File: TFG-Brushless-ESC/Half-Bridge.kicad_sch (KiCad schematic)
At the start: 19 parts, among them Q5 TK58E06N1, Q6 TK58E06N1, U8 IR2101, U9 INA180A3

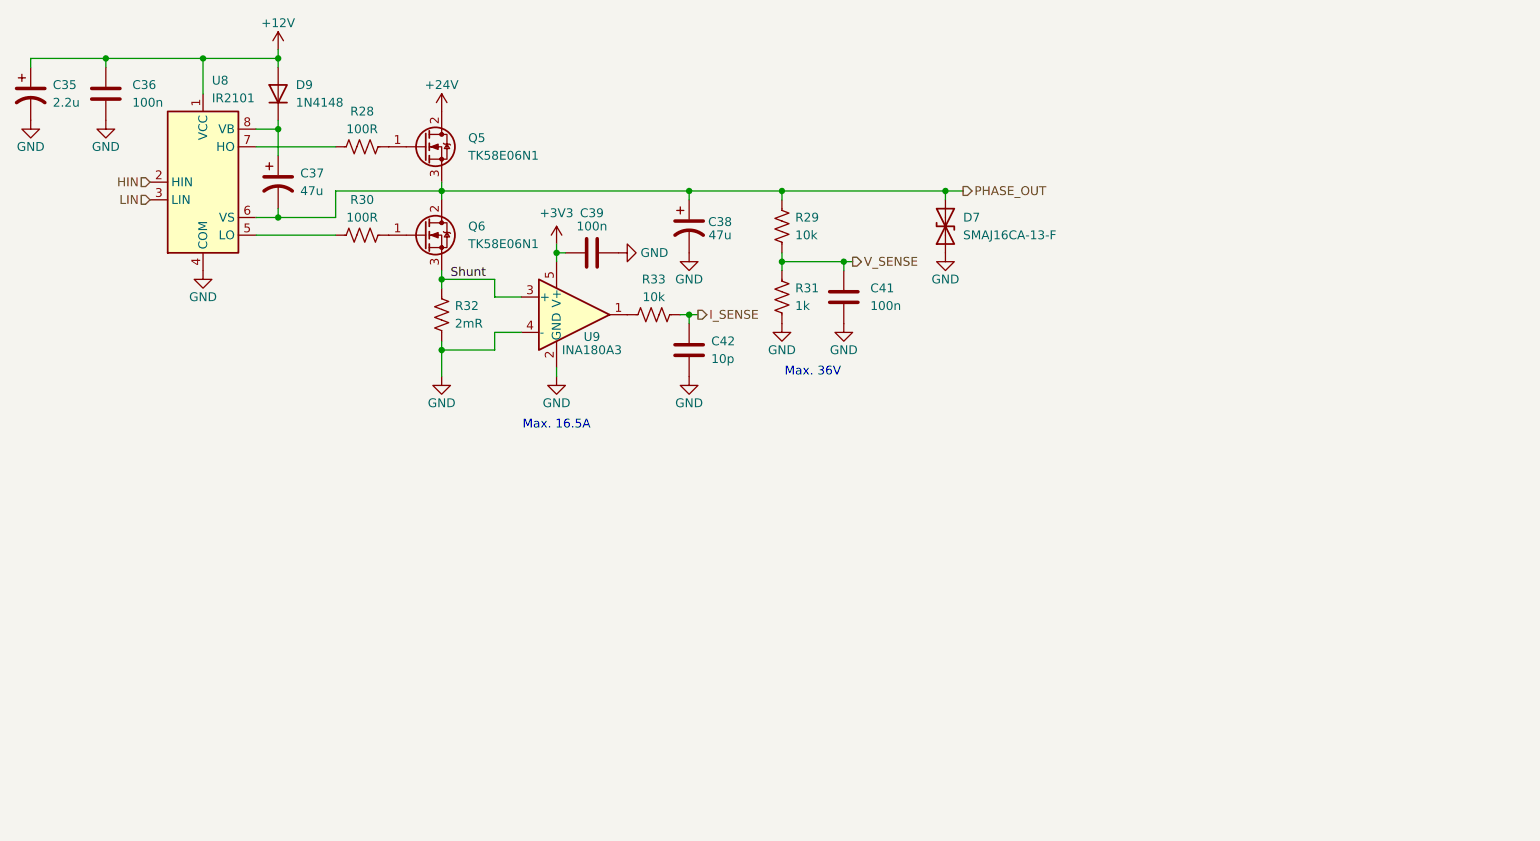
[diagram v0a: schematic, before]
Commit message: updated code to match pinout
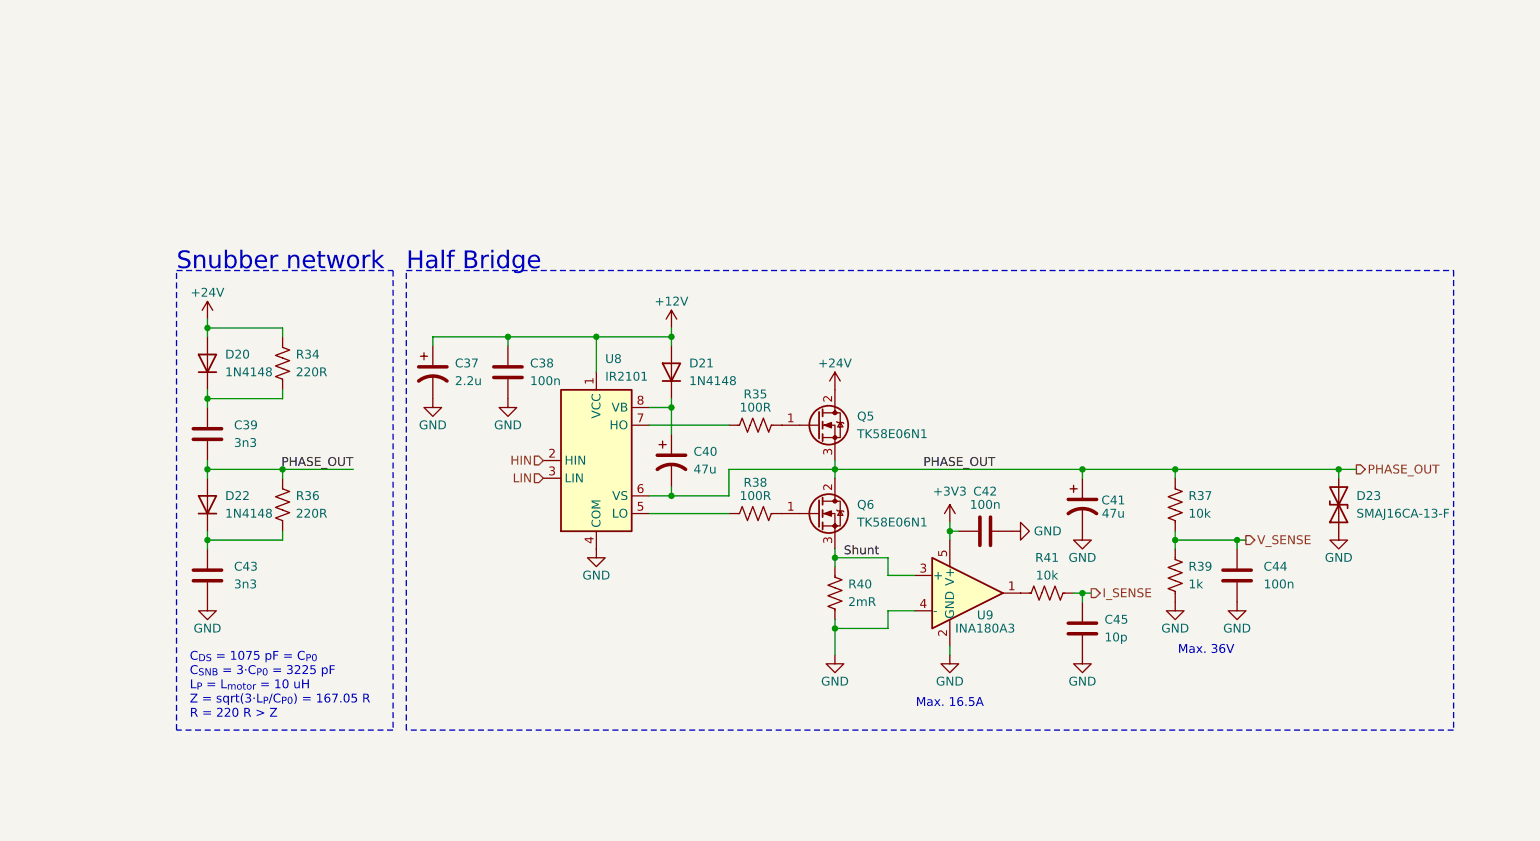
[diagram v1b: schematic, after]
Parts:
- added C39, C43: 3n3, Capacitor_SMD:C_0603_1608Metric, symbol Device:C
- added D20, D22: 1N4148, Diode_SMD:D_SOD-123, symbol Device:D
- added R34, R36: 220R, Resistor_SMD:R_0603_1608Metric, symbol Device:R_US
- C37: renamed from C35; footprint Capacitor_THT:CP_Radial_D5.0mm_P2.00mm -> Capacitor_SMD:CP_Elec_4x5.4
- C40: renamed from C37; footprint Capacitor_THT:CP_Radial_D5.0mm_P2.00mm -> Capacitor_SMD:CP_Elec_4x5.4
- C41: renamed from C38; footprint Capacitor_THT:CP_Radial_D5.0mm_P2.00mm -> Capacitor_SMD:CP_Elec_4x5.4
- renumbered C36 to C38, C39 to C42, C41 to C44, C42 to C45, D9 to D21, D7 to D23, R28 to R35, R29 to R37, R30 to R38, R31 to R39, R32 to R40, R33 to R41
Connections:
- net +24V: now also D20.2 (A), R34.2
- net GND: now also C43.2
- net PHASE_OUT: now also C39.2, D22.2 (A), R36.2
- new net: C43.1, D22.1 (K), R36.1
- new net: C39.1, D20.1 (K), R34.1
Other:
- note added: "C_{DS} = 1075 pF = C_{P0} C_{SNB} = 3·C_{P0} = 3225 pF L_{P} = L_{motor} = 10 uH Z = sqrt(3·L_{P}/C_{P0}) = 167.05 R R = 220 R > Z"
- note added: "Half Bridge"
- note added: "Snubber network"
- moved on the sheet: C37, C38, C40, C41, C42, C44, C45, D21, D23, Q5, Q6, R35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

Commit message: Slight code changes
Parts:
- removed C41: 47u, Capacitor_SMD:CP_Elec_4x5.4, symbol Device:C_Polarized_US
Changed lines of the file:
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@@
 	)
 	(junction
-		(at 186.69 94.615)
-		(diameter 0)
-		(color 0 0 0 0)
-	)
-	(junction
 		(at 127.635 98.425)
 		(diameter 0)
@@
 	(wire
 		(pts
-			(xy 151.13 94.615) (xy 186.69 94.615)
-		)
-		(stroke
-			(width 0)
-			(type default)
-		)
-	)
-	(wire
-		(pts
 			(xy 71.755 74.295) (xy 60.96 74.295)
 		)
@@
 	(wire
 		(pts
-			(xy 186.69 94.615) (xy 200.025 94.615)
+			(xy 151.13 94.615) (xy 200.025 94.615)
 		)
 		(stroke
@@
 	(wire
 		(pts
-			(xy 186.69 94.615) (xy 186.69 95.885)
-		)
-		(stroke
-			(width 0)
-			(type default)
-		)
-	)
-	(wire
-		(pts
 			(xy 200.025 94.615) (xy 223.52 94.615)
 		)
@@
 	(symbol
 		(lib_id "power:GND")
-		(at 186.69 103.505 0)
-		(unit 1)
-		(exclude_from_sim no)
-		(in_bom yes)
-		(on_board yes)
-		(dnp no)
-		(property "Reference" "#PWR098"
-			(at 186.69 109.855 0)
-			(effects
-				(font
-					(size 1.27 1.27)
-				)
-				(hide yes)
-			)
-		)
-		(property "Value" "GND"
-			(at 186.69 107.315 0)
-			(effects
-				(font
-					(size 1.27 1.27)
-				)
-			)
-		)
-		(property "Footprint" ""
-			(at 186.69 103.505 0)
-			(effects
-				(font
-					(size 1.27 1.27)
-				)
-				(hide yes)
-			)
-		)
-		(property "Datasheet" ""
-			(at 186.69 103.505 0)
-			(effects
-				(font
-					(size 1.27 1.27)
-				)
-				(hide yes)
-			)
-		)
-		(property "Description" ""
-			(at 186.69 103.505 0)
-			(effects
-				(font
-					(size 1.27 1.27)
-				)
-				(hide yes)
-			)
-		)
-		(pin "1"
-		)
-		(instances
-			(project "TFG-Brushless-ESC"
-				(path "/fc8dd9a9-f99a-4338-8182-2c8b4b8ed6dd/211b6883-96c8-42a2-bec5-a4dfd4e56ba6"
-					(reference "#PWR098")
-					(unit 1)
-				)
-				(path "/fc8dd9a9-f99a-4338-8182-2c8b4b8ed6dd/b5458e57-2ddd-4d30-9620-d640c1a391c8"
-					(reference "#PWR066")
-					(unit 1)
-				)
-				(path "/fc8dd9a9-f99a-4338-8182-2c8b4b8ed6dd/f6e668ab-a50d-4861-bee8-58a57ed6fcc7"
-					(reference "#PWR082")
-					(unit 1)
-				)
-			)
-		)
-	)
-	(symbol
-		(lib_id "power:GND")
 		(at 60.96 113.665 0)
 		(unit 1)
@@
 					(unit 1)
 				)
-			)
-		)
-	)
-	(symbol
-		(lib_id "Device:C_Polarized_US")
-		(at 186.69 99.695 0)
-		(unit 1)
-		(exclude_from_sim no)
-		(in_bom yes)
-		(on_board yes)
-		(dnp no)
-		(property "Reference" "C41"
-			(at 191.135 99.06 0)
-			(effects
-				(font
-					(size 1.27 1.27)
-				)
-			)
-		)
-		(property "Value" "47u"
-			(at 191.135 100.965 0)
-			(effects
-				(font
-					(size 1.27 1.27)
-				)
-			)
-		)
-		(property "Footprint" "Capacitor_SMD:CP_Elec_4x5.4"
-			(at 186.69 99.695 0)
-			(effects
-				(font
-					(size 1.27 1.27)
-				)
-				(hide yes)
-			)
-		)
-		(property "Datasheet" "~"
-			(at 186.69 99.695 0)
-			(effects
-				(font
-					(size 1.27 1.27)
-				)
-				(hide yes)
-			)
-		)
-		(property "Description" ""
-			(at 186.69 99.695 0)
-			(effects
-				(font
-					(size 1.27 1.27)
-				)
-				(hide yes)
-			)
-		)
-		(property "Sim.Device" "C"
-			(at 186.69 99.695 0)
-			(effects
-				(font
-					(size 1.27 1.27)
-				)
-				(hide yes)
-			)
-		)
-		(property "Sim.Pins" "1=+ 2=-"
-			(at 186.69 99.695 0)
-			(effects
-				(font
-					(size 1.27 1.27)
-				)
-				(hide yes)
-			)
-		)
-		(pin "1"
-		)
-		(pin "2"
-		)
-		(instances
-			(project "TFG-Brushless-ESC"
-				(path "/fc8dd9a9-f99a-4338-8182-2c8b4b8ed6dd/211b6883-96c8-42a2-bec5-a4dfd4e56ba6"
-					(reference "C41")
-					(unit 1)
-				)
-				(path "/fc8dd9a9-f99a-4338-8182-2c8b4b8ed6dd/b5458e57-2ddd-4d30-9620-d640c1a391c8"
-					(reference "C23")
-					(unit 1)
-				)
-				(path "/fc8dd9a9-f99a-4338-8182-2c8b4b8ed6dd/f6e668ab-a50d-4861-bee8-58a57ed6fcc7"
-					(reference "C32")
-					(unit 1)
-				)

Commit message: PCB v3
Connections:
- net VB: now reaches C40.1, D21.1 (K), U8.8 (VB)
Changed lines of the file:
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@@
+		)
+	)
+	(label "VB"
+		(at 125.095 85.725 0)
+		(effects
+			(font
+				(size 1.27 1.27)
+			)
+			(justify left bottom)
 		)
 	)

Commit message: Added fan control and temp measurement. Not added to pcb yet
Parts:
- added J6: ~, TFG-Brushless-ESC:Screw_Terminal, symbol Connector:Screw_Terminal_01x01
- added R42: 10k, Resistor_SMD:R_0603_1608Metric, symbol Device:R_US
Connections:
- net GND: now also R42.1
- net PHASE_OUT: now also J6.1 (Pin_1), R42.2

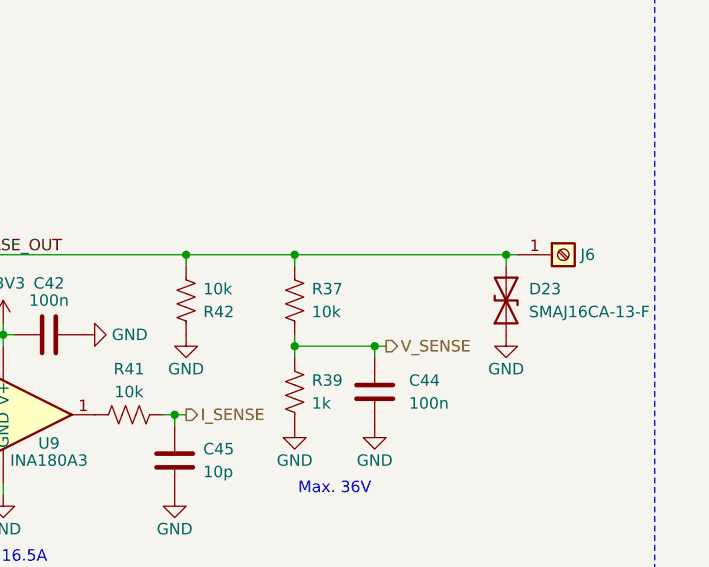
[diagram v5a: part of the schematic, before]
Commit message: Added temperature sensors per phase and adc
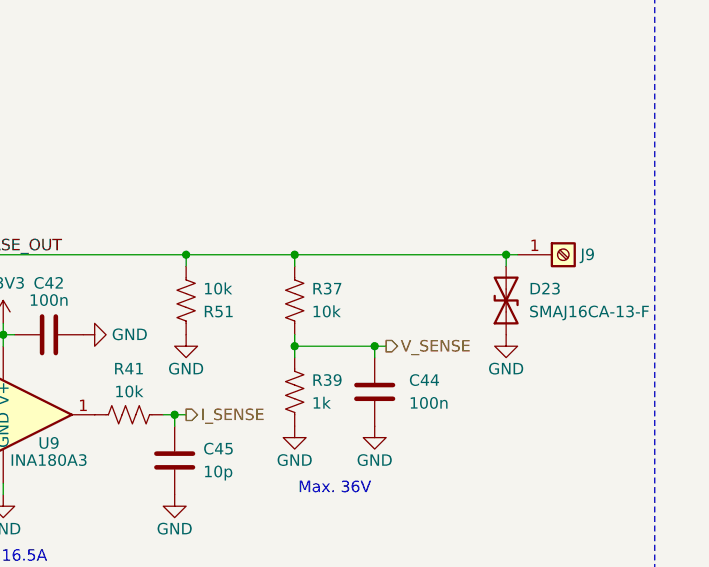
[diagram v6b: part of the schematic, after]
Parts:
- renumbered J6 to J9, R42 to R51
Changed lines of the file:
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@@
 		(on_board yes)
 		(dnp no)
-		(property "Reference" "#PWR0118"
+		(property "Reference" "#PWR0120"
 			(at 187.96 109.855 0)
 			(effects
@@
 		(on_board yes)
 		(dnp no)
-		(property "Reference" "J6"
+		(property "Reference" "J9"
 			(at 231.775 94.615 0)
 			(effects
@@
 		(on_board yes)
 		(dnp no)
-		(property "Reference" "R42"
+		(property "Reference" "R51"
 			(at 189.865 100.965 0)
 			(effects

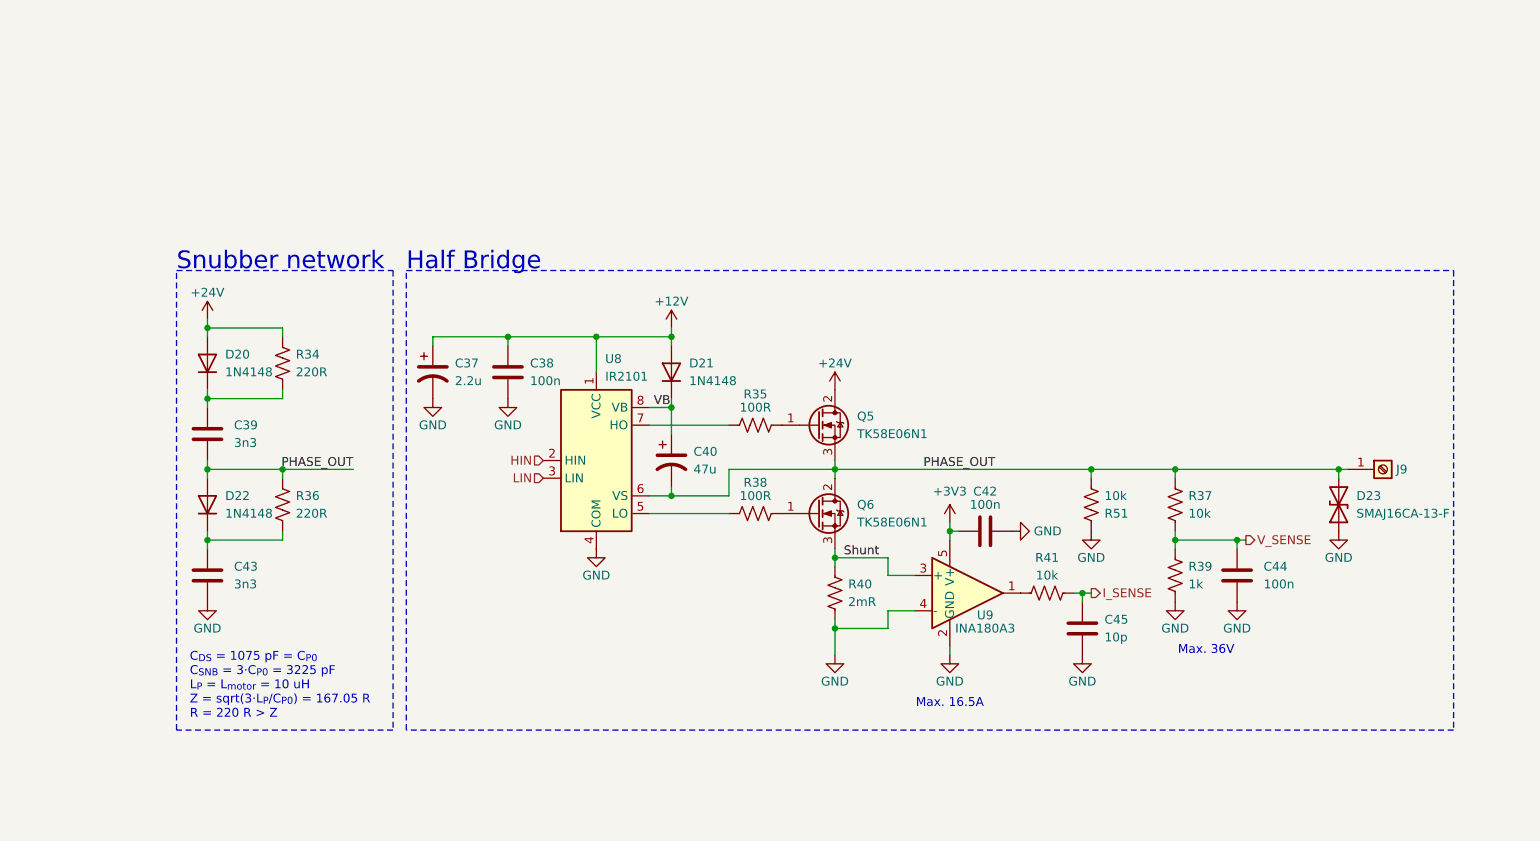
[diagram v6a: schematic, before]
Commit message: Added pulldown resistors for the half bridge mosfets, fan mosfet and fixed code pinout
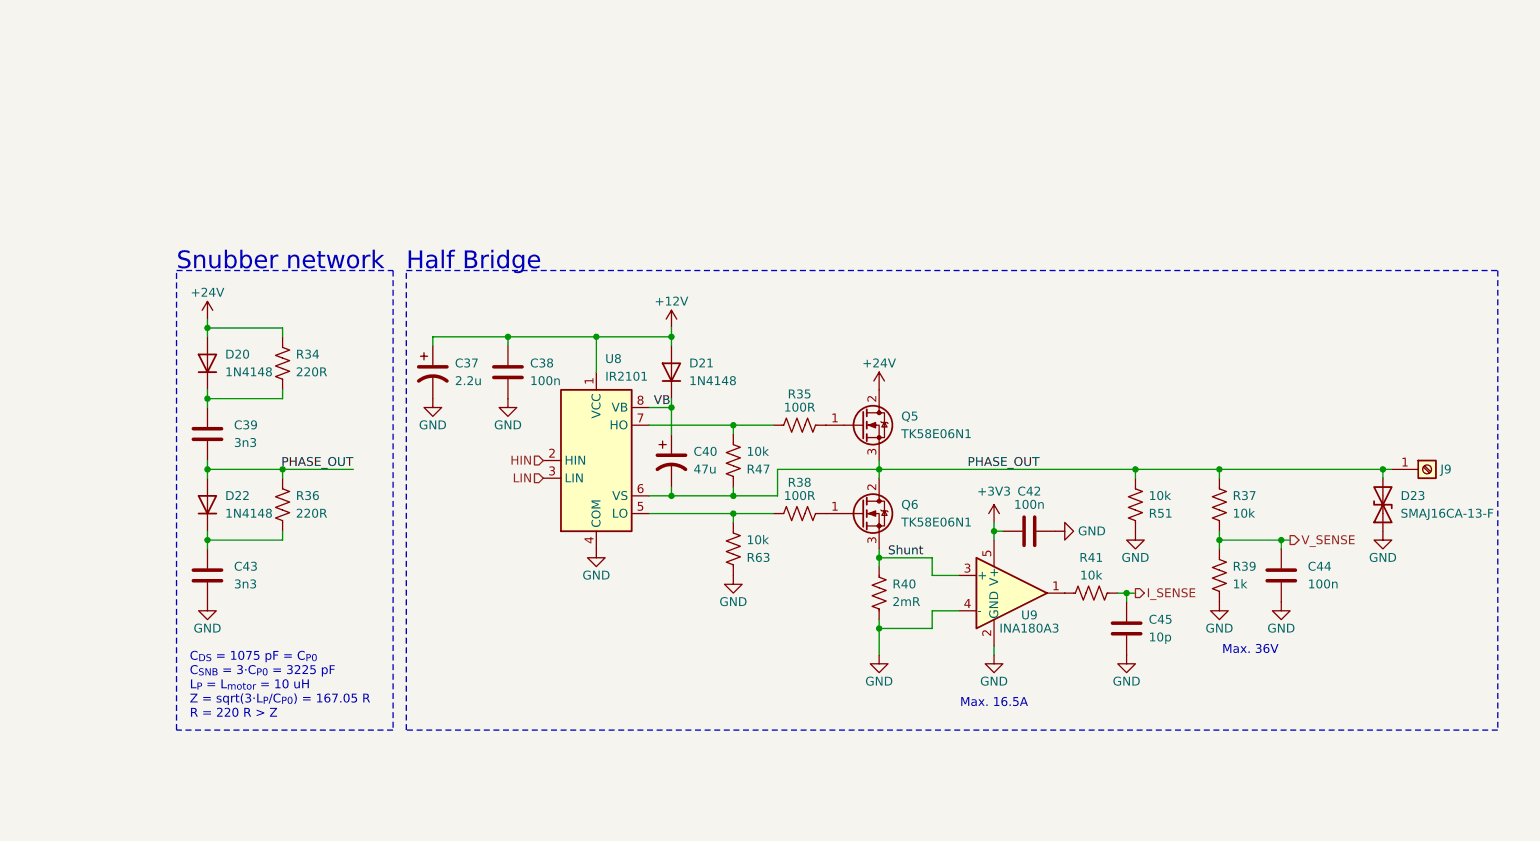
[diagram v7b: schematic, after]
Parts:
- added R47, R63: 10k, Resistor_SMD:R_0603_1608Metric, symbol Device:R_US
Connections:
- net GND: now also R63.1
- net PHASE_OUT: now also R47.1
- net at R38.1, U8.5 (LO): now also R63.2
- net at R35.1, U8.7 (HO): now also R47.2
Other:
- moved on the sheet: C42, C44, C45, D23, J9, Q5, Q6, R35, R37, R38, R39, R40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

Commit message: Traducción nombres
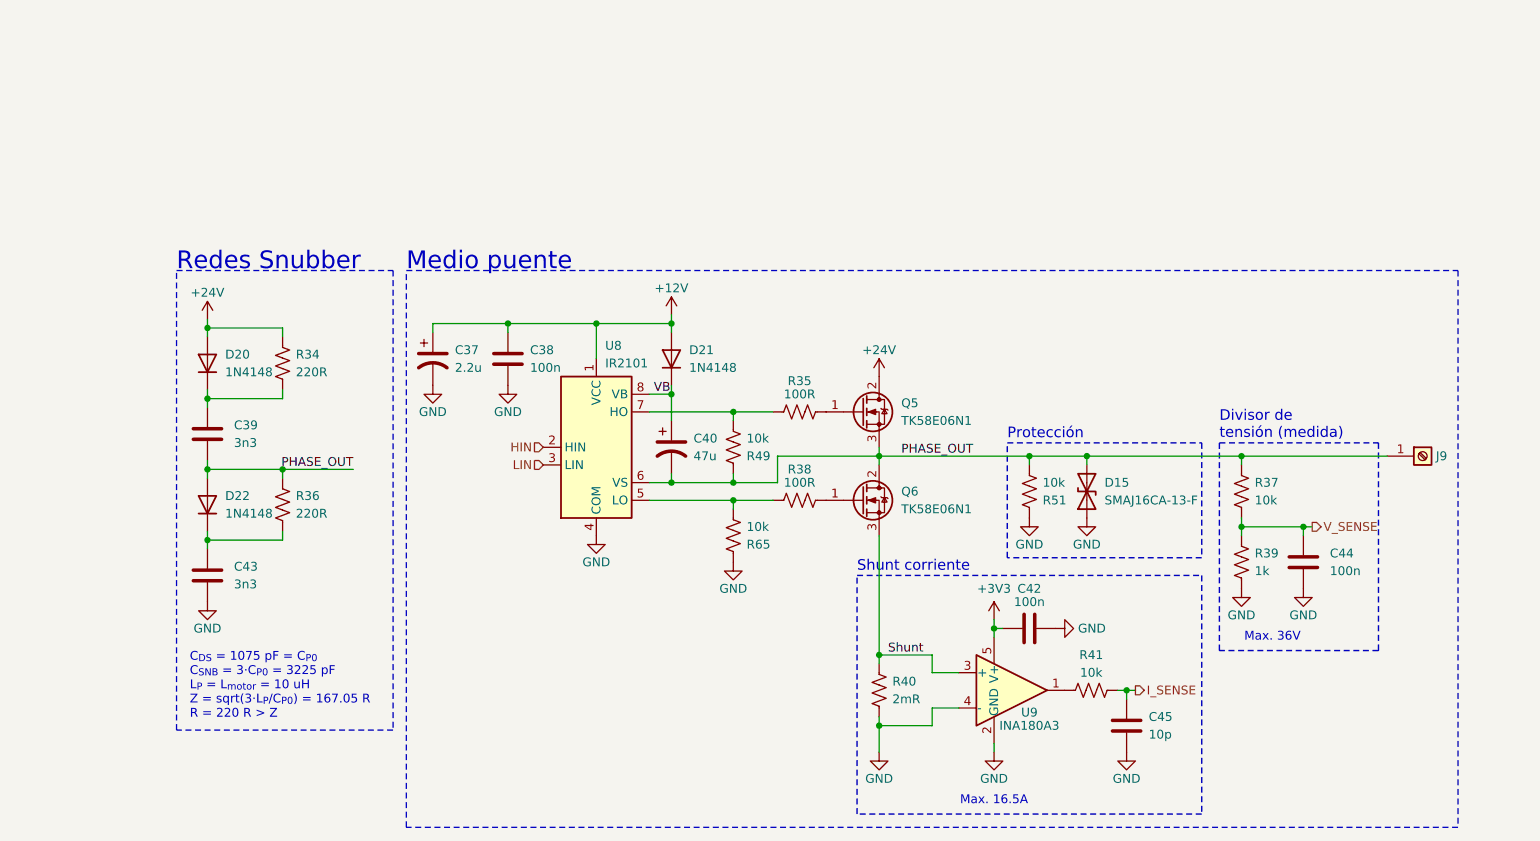
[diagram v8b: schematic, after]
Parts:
- removed D23: SMAJ16CA-13-F, Diode_SMD:D_SMA, symbol Device:D_TVS
- added D15: SMAJ16CA-13-F, Diode_SMD:D_SMA, symbol Device:D_TVS
- renumbered R47 to R49, R63 to R65
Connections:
- net GND: now also D15.1 (A1)
- net PHASE_OUT: now also D15.2 (A2)
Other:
- note added: "Divisor de tensión (medida)"
- note added: "Medio puente"
- note added: "Protección"
- note added: "Redes Snubber"
- note added: "Shunt corriente"
- note removed: "Half Bridge"
- note removed: "Snubber network"
- moved on the sheet: C37, C38, C40, C42, C44, C45, D21, J9, Q5, Q6, R35, R37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
